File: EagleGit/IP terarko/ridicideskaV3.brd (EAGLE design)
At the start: 142.2 x 94.9 mm, 59 parts, among them IC1 74HC595N, IC2 74HC597N, Q3 32.768kHz

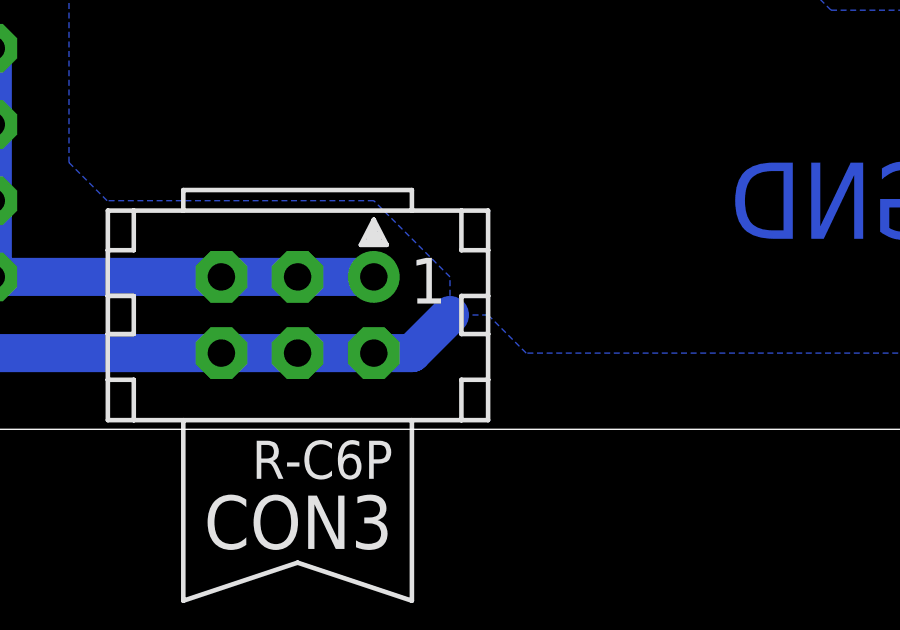
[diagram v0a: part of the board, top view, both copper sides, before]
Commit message: Terarko: - pridadana dokumentace k procesoru a modulu bluetooth - upravena funkce kernelu = scheduler tak, aby mazala vlajku preruseni - inicializace vlaken presunuta do Peripheral.c
- odzkouseno, vlakna chodi spravne.
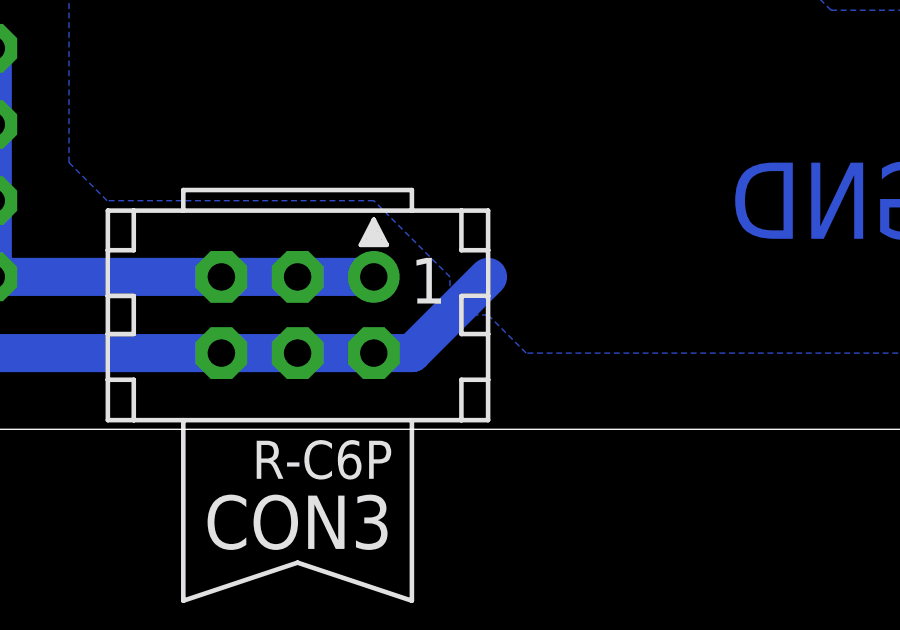
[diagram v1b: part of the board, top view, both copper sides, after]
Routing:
- net GND: track 281.1 -> 282.9 mm
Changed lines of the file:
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@@
 <?xml version="1.0" encoding="utf-8"?>
 <!DOCTYPE eagle SYSTEM "eagle.dtd">
-<eagle version="6.3">
+<eagle version="7.2.0">
 <drawing>
 <settings>
@@
 <layer number="19" name="Unrouted" color="6" fill="1" visible="yes" active="yes"/>
 <layer number="20" name="Dimension" color="15" fill="1" visible="yes" active="yes"/>
-<layer number="21" name="tPlace" color="7" fill="1" visible="no" active="yes"/>
-<layer number="22" name="bPlace" color="7" fill="1" visible="no" active="yes"/>
-<layer number="23" name="tOrigins" color="15" fill="1" visible="no" active="yes"/>
-<layer number="24" name="bOrigins" color="15" fill="1" visible="no" active="yes"/>
-<layer number="25" name="tNames" color="7" fill="1" visible="no" active="yes"/>
-<layer number="26" name="bNames" color="7" fill="1" visible="no" active="yes"/>
-<layer number="27" name="tValues" color="7" fill="1" visible="no" active="yes"/>
-<layer number="28" name="bValues" color="7" fill="1" visible="no" active="yes"/>
+<layer number="21" name="tPlace" color="7" fill="1" visible="yes" active="yes"/>
+<layer number="22" name="bPlace" color="7" fill="1" visible="yes" active="yes"/>
+<layer number="23" name="tOrigins" color="15" fill="1" visible="yes" active="yes"/>
+<layer number="24" name="bOrigins" color="15" fill="1" visible="yes" active="yes"/>
+<layer number="25" name="tNames" color="7" fill="1" visible="yes" active="yes"/>
+<layer number="26" name="bNames" color="7" fill="1" visible="yes" active="yes"/>
+<layer number="27" name="tValues" color="7" fill="1" visible="yes" active="yes"/>
+<layer number="28" name="bValues" color="7" fill="1" visible="yes" active="yes"/>
 <layer number="29" name="tStop" color="7" fill="3" visible="no" active="yes"/>
 <layer number="30" name="bStop" color="7" fill="6" visible="no" active="yes"/>
@@
 <layer number="49" name="Reference" color="7" fill="1" visible="no" active="yes"/>
 <layer number="50" name="dxf" color="7" fill="1" visible="no" active="no"/>
-<layer number="51" name="tDocu" color="7" fill="1" visible="no" active="yes"/>
-<layer number="52" name="bDocu" color="7" fill="1" visible="no" active="yes"/>
+<layer number="51" name="tDocu" color="7" fill="1" visible="yes" active="yes"/>
+<layer number="52" name="bDocu" color="7" fill="1" visible="yes" active="yes"/>
 <layer number="53" name="tGND_GNDA" color="7" fill="9" visible="no" active="no"/>
 <layer number="54" name="bGND_GNDA" color="1" fill="9" visible="no" active="no"/>
 <layer number="56" name="wert" color="7" fill="1" visible="no" active="no"/>
 <layer number="57" name="tCAD" color="7" fill="1" visible="no" active="no"/>
-<layer number="90" name="Modules" color="5" fill="1" visible="no" active="yes"/>
+<layer number="90" name="Modules" color="5" fill="1" visible="no" active="no"/>
 <layer number="91" name="Nets" color="2" fill="1" visible="no" active="no"/>
 <layer number="92" name="Busses" color="1" fill="1" visible="no" active="no"/>
@@
 <wire x1="142.22" y1="94.92" x2="0" y2="94.92" width="0" layer="20"/>
 <wire x1="0" y1="94.92" x2="0" y2="0" width="0" layer="20"/>
-<dimension x1="0" y1="0" x2="142.24" y2="0" x3="71.12" y3="-20.32" layer="48"/>
-<dimension x1="126.365" y1="5.08" x2="126.365" y2="90.17" x3="157.48" y3="47.625" layer="48"/>
-<dimension x1="142.22" y1="0" x2="142.22" y2="94.92" x3="166.37" y3="47.46" layer="48"/>
+<dimension x1="0" y1="0" x2="142.24" y2="0" x3="71.12" y3="-20.32" textsize="3.5" layer="48"/>
+<dimension x1="126.365" y1="5.08" x2="126.365" y2="90.17" x3="157.48" y3="47.625" textsize="3.5" layer="48"/>
+<dimension x1="142.22" y1="0" x2="142.22" y2="94.92" x3="166.37" y3="47.46" textsize="3.5" layer="48"/>
 <text x="40.64" y="73.66" size="2.54" layer="16" rot="MR0">BLUETOOTH KIT
 modul: RN-41
 proc: STM8S Discovery</text>
 <text x="102.87" y="6.35" size="2.54" layer="16" rot="MR0">GND</text>
-<dimension x1="5.08" y1="5.08" x2="120.015" y2="5.08" x3="62.5475" y3="-10.16" layer="48"/>
+<dimension x1="5.08" y1="5.08" x2="120.015" y2="5.08" x3="62.5475" y3="-10.16" textsize="3.5" layer="48"/>
 </plain>
 <attributes>
@@
 <pass name="Default">
 <param name="RoutingGrid" value="50mil"/>
+<param name="AutoGrid" value="1"/>
+<param name="Efforts" value="0"/>
+<param name="TopRouterVariant" value="1"/>
 <param name="tpViaShape" value="round"/>
 <param name="PrefDir.1" value="|"/>
@@
 <wire x1="81.28" y1="2.54" x2="83.82" y2="2.54" width="1.27" layer="16"/>
 <wire x1="83.82" y1="2.54" x2="85.09" y2="2.54" width="1.27" layer="16"/>
-<wire x1="85.09" y1="2.54" x2="86.36" y2="3.81" width="1.27" layer="16"/>
+<wire x1="85.09" y1="2.54" x2="87.63" y2="5.08" width="1.27" layer="16"/>
 <contactref element="C18" pad="2"/>
 <contactref element="C19" pad="2"/>

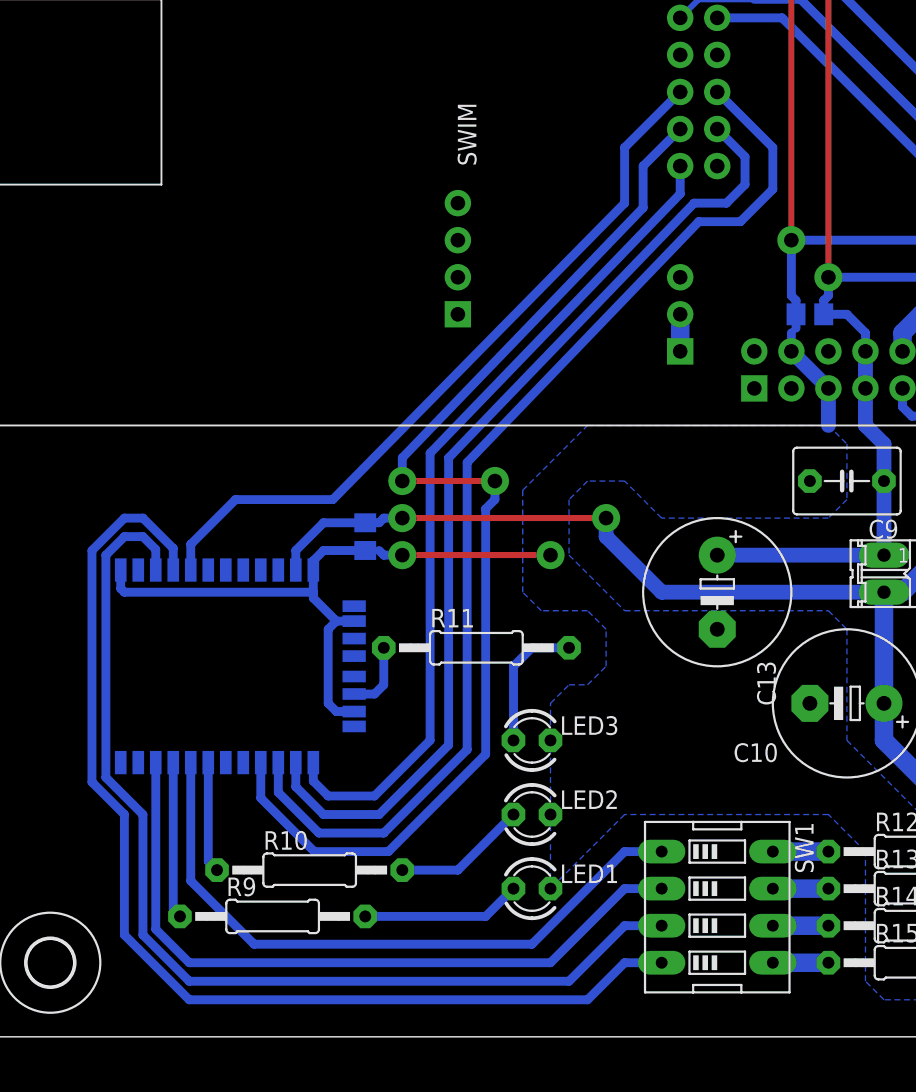
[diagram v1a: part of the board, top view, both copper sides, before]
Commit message: Terarko: - chyba na ridici desce, byly prohozeny TX a RX privody k bluetooth modulu.
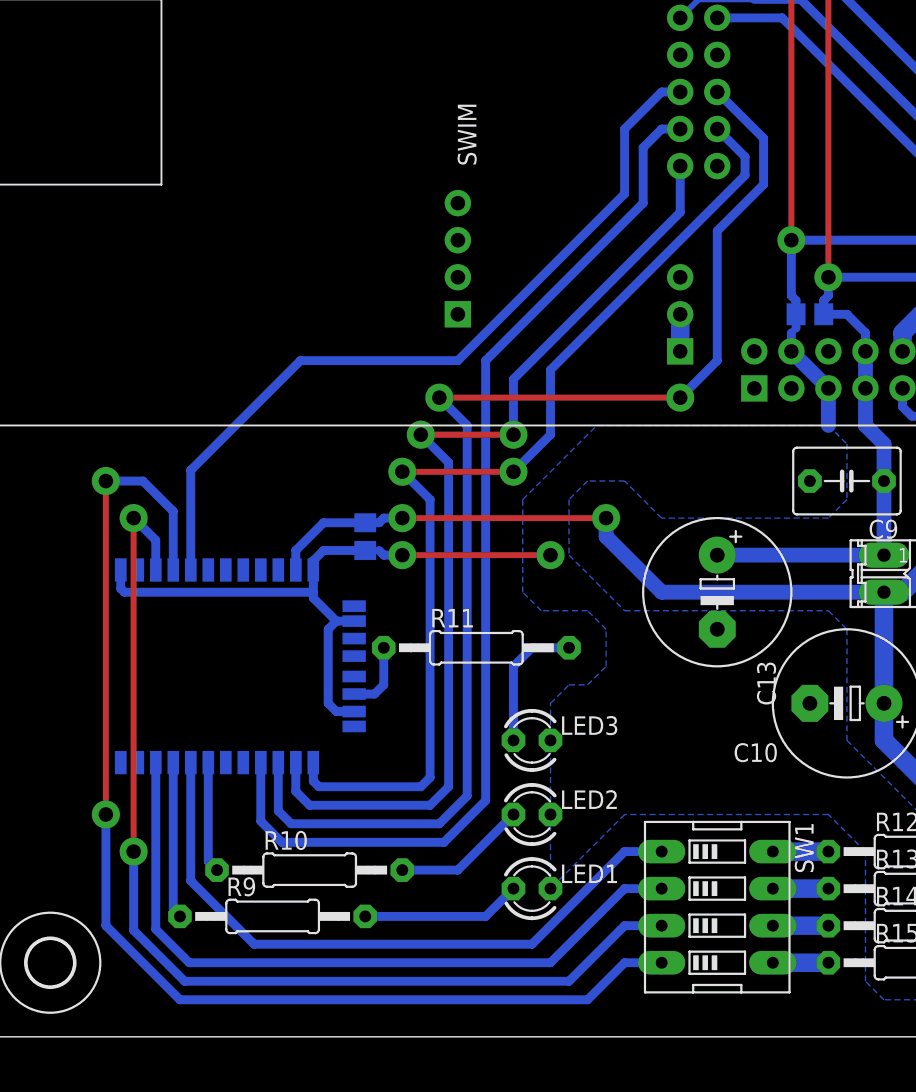
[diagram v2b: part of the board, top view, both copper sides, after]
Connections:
- net N$47: now also U$1.13; no longer U$1.14
- net N$48: now also U$1.14; no longer U$1.13
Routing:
- net N$64: track 75.3 -> 86.7 mm, vias 0 -> 2
- net N$48: track 57.6 -> 67.8 mm, vias 0 -> 2
- net N$63: track 79.3 -> 73.5 mm, vias 2 -> 0
- net N$56: track 75.8 -> 81.2 mm, vias 0 -> 2
- net N$69: track 50.5 -> 53.7 mm
- net N$47: track 67.4 -> 69.9 mm, vias 0 -> 2
- net N$55: track 71.3 -> 71.7 mm, vias 0 -> 2

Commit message: Terarko: - do cesty Rx, CTS pridany 1k rezistory
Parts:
- added R18, R19: 1k, rcl:0207/12
- moved R11 1.90 mm to (34.3, 28.6)
- moved R10 1.27 mm to (24.1, 11.4)
- moved R9 0.63 mm to (21.0, 8.26)
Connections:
- new net N$42: R19.1, U$1.13
- new net N$65: R18.1, U$1.16
- net N$47: now also R19.2; no longer U$1.13
- net N$63: now also R18.2; no longer U$1.16
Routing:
- net N$47: track 69.9 -> 29.0 mm, vias 2 -> 0
- net N$42: track 0.00 -> 36.1 mm
- net N$63: track 73.5 -> 42.6 mm
- net N$65: track 0.00 -> 17.7 mm
- net N$64: track 86.7 -> 76.1 mm, vias 2 -> 0
- net N$48: track 67.8 -> 61.3 mm, vias 2 -> 0
- net N$57: track 4.83 -> 6.74 mm
- net N$52: track 9.20 -> 7.93 mm
- net N$49: track 10.9 -> 10.3 mm
- net N$51: track 7.62 -> 8.14 mm

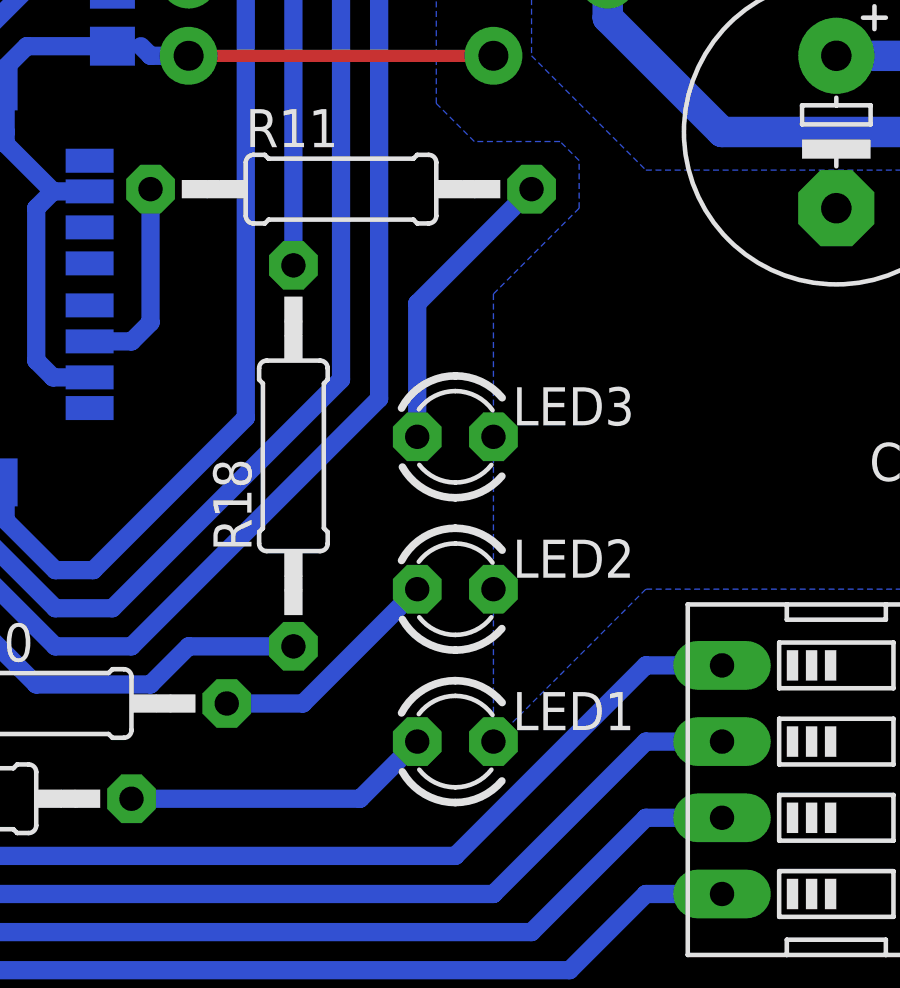
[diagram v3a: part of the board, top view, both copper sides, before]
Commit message: Terarko: - zvetseny prostor pro diody
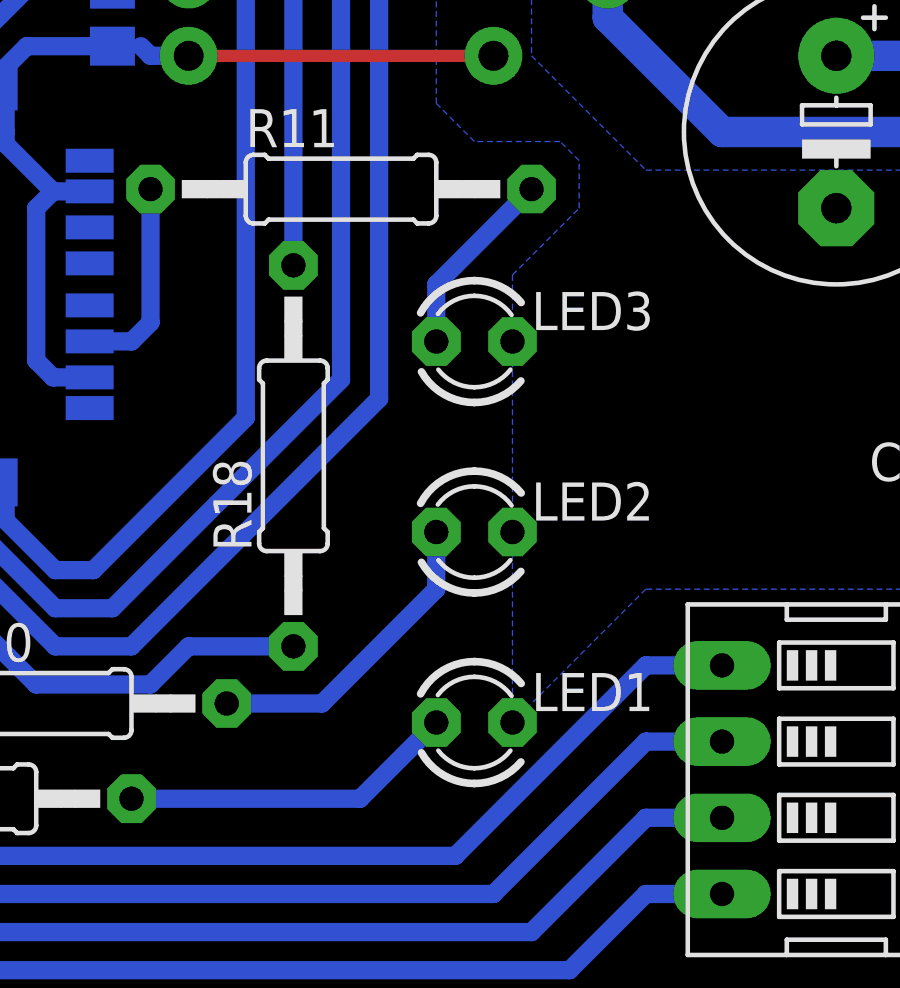
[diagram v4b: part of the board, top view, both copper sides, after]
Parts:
- moved LED3 3.24 mm to (38.7, 23.5)
- moved LED2 2.01 mm to (38.7, 17.1)
- moved LED1 0.90 mm to (38.7, 10.8)
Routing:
- net N$58: track 9.83 -> 6.40 mm
- net N$52: track 7.93 -> 10.5 mm
- net N$49: track 10.3 -> 11.2 mm
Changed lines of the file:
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@@
 <element name="U$1" library="SparkFun-RF" package="RN41" value="BLUETOOTH-RN41&quot;" x="16.51" y="25.4" rot="MR180"/>
 <element name="R9" library="rcl" package="0207/12" value="220R" x="20.955" y="8.255"/>
-<element name="LED1" library="led" package="LED3MM" value="" x="38.1" y="10.16"/>
+<element name="LED1" library="led" package="LED3MM" value="" x="38.735" y="10.795"/>
 <element name="R10" library="rcl" package="0207/12" value="220R" x="24.13" y="11.43"/>
-<element name="LED2" library="led" package="LED3MM" value="" x="38.1" y="15.24"/>
+<element name="LED2" library="led" package="LED3MM" value="" x="38.735" y="17.145"/>
 <element name="SW1" library="special" package="EDG-04" value="" x="50.8" y="8.89" rot="R270"/>
 <element name="R11" library="rcl" package="0207/12" value="220R" x="34.29" y="28.575"/>
-<element name="LED3" library="led" package="LED3MM" value="" x="38.1" y="20.32"/>
+<element name="LED3" library="led" package="LED3MM" value="" x="38.735" y="23.495"/>
 <element name="R12" library="rcl" package="0207/12" value="1k" x="64.77" y="12.7"/>
 <element name="R13" library="rcl" package="0207/12" value="1k" x="64.77" y="10.16"/>
@@
 <wire x1="23.11" y1="30.48" x2="23.11" y2="32" width="0.6096" layer="16"/>
 <polygon width="0.4064" layer="16">
-<vertex x="39.37" y="10.16"/>
-<vertex x="39.37" y="25.0825"/>
+<vertex x="40.005" y="10.795"/>
+<vertex x="40.005" y="25.7175"/>
 <vertex x="42.2275" y="27.94"/>
 <vertex x="42.2275" y="29.5275"/>
@@
 <contactref element="R9" pad="2"/>
 <wire x1="27.305" y1="8.255" x2="34.925" y2="8.255" width="0.6096" layer="16"/>
-<wire x1="34.925" y1="8.255" x2="36.83" y2="10.16" width="0.6096" layer="16"/>
+<wire x1="34.925" y1="8.255" x2="37.465" y2="10.795" width="0.6096" layer="16"/>
 </signal>
 <signal name="N$50">
@@
 <contactref element="R10" pad="2"/>
 <contactref element="LED2" pad="A"/>
-<wire x1="30.48" y1="11.43" x2="33.02" y2="11.43" width="0.6096" layer="16"/>
-<wire x1="33.02" y1="11.43" x2="36.83" y2="15.24" width="0.6096" layer="16"/>
+<wire x1="30.48" y1="11.43" x2="33.655" y2="11.43" width="0.6096" layer="16"/>
+<wire x1="33.655" y1="11.43" x2="37.465" y2="15.24" width="0.6096" layer="16"/>
+<wire x1="37.465" y1="15.24" x2="37.465" y2="17.145" width="0.6096" layer="16"/>
 </signal>
 <signal name="N$53">
@@
 <contactref element="R11" pad="2"/>
 <contactref element="LED3" pad="A"/>
-<wire x1="36.83" y1="20.32" x2="36.83" y2="24.765" width="0.6096" layer="16"/>
-<wire x1="36.83" y1="24.765" x2="40.64" y2="28.575" width="0.6096" layer="16"/>
+<wire x1="37.465" y1="23.495" x2="37.465" y2="25.4" width="0.6096" layer="16"/>
+<wire x1="37.465" y1="25.4" x2="40.64" y2="28.575" width="0.6096" layer="16"/>
 </signal>
 <signal name="N$59">
